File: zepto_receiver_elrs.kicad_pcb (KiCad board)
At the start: 4 copper layers, 11.2 x 7.5 mm, 44 parts, among them J1 u.fl, SW1 SW_Push, U1 STM32WLE5JBI6, U2 NCP160, U3 BGS12PL6E6327XTSA1, U4 0900FM15D0039, U5 ECS-TXO-25CSMV-320-AM-TR

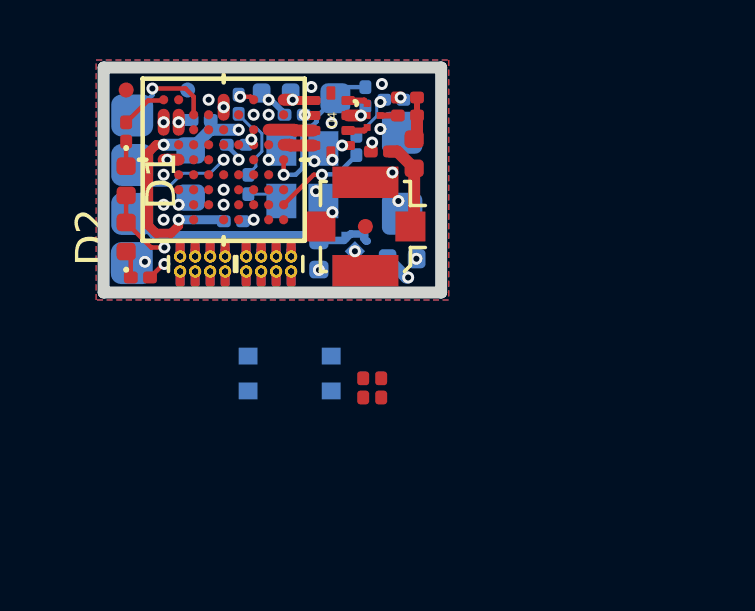
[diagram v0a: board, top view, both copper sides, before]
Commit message: updated silk screen
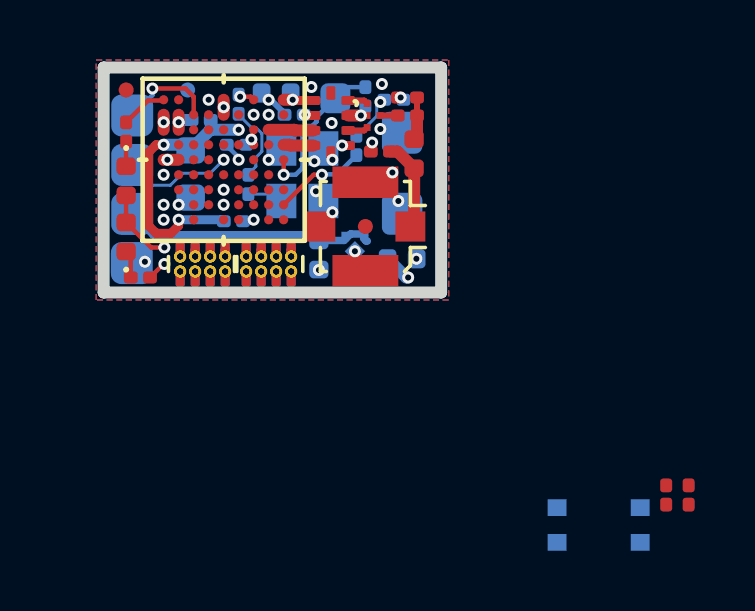
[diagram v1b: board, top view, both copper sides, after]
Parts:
- moved SW1 11.5 mm to (136.5, 66.2)
- moved R3 10.9 mm to (139.5, 65.2)
- moved C4 10.7 mm to (138.8, 65.2)
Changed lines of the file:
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@@
   (module ftprnts:0900FM15D0039 (layer F.Cu)
     (at 127.575 52.85 90)
-    (fp_text reference U4 (at 0.1 0.05 90) (layer F.SilkS)
+    (fp_text reference U4 (at 0.1 0.05 90) (layer F.SilkS) hide
       (effects (font (size 0.3 0.3) (thickness 0.05)))
     )
-    (fp_text value 0900FM15D0039 (at -0.1 -0.05 90) (layer F.Fab)
+    (fp_text value 0900FM15D0039 (at -0.1 -0.05 90) (layer F.Fab) hide
       (effects (font (size 1 1) (thickness 0.15)))
     )
@@
     (tags "SMD SMT crystal")
     (attr smd)
-    (fp_text reference U5 (at 0 2.2 90) (layer B.SilkS)
-      (effects (font (size 1 1) (thickness 0.15)) (justify mirror))
-    )
-    (fp_text value ECS-TXO-25CSMV-320-AM-TR (at 0 -2.2 90) (layer B.Fab)
+    (fp_text reference U5 (at 0 2.2 90) (layer B.SilkS) hide
+      (effects (font (size 1 1) (thickness 0.15)) (justify mirror))
+    )
+    (fp_text value ECS-TXO-25CSMV-320-AM-TR (at 0 -2.2 90) (layer B.Fab) hide
       (effects (font (size 1 1) (thickness 0.15)) (justify mirror))
     )
@@
     (fp_line (start 1.15 1) (end 1.25 0.9) (layer B.Fab) (width 0.1))
     (fp_line (start -1.15 1) (end 1.15 1) (layer B.Fab) (width 0.1))
-    (fp_text user %R (at 0 0 90) (layer B.Fab)
+    (fp_text user %R (at 0 0 90) (layer B.Fab) hide
       (effects (font (size 0.6 0.6) (thickness 0.09)) (justify mirror))
     )
@@
     (tags resistor)
     (attr smd)
-    (fp_text reference R6 (at 0 1.05 90) (layer B.SilkS)
-      (effects (font (size 1 1) (thickness 0.15)) (justify mirror))
-    )
-    (fp_text value 220R (at 0 -1.05 90) (layer B.Fab)
+    (fp_text reference R6 (at 0 1.05 90) (layer B.SilkS) hide
+      (effects (font (size 1 1) (thickness 0.15)) (justify mirror))
+    )
+    (fp_text value 220R (at 0 -1.05 90) (layer B.Fab) hide
       (effects (font (size 1 1) (thickness 0.15)) (justify mirror))
     )
@@
     (fp_line (start 0.65 0.3) (end 0.65 -0.3) (layer B.CrtYd) (width 0.05))
     (fp_line (start 0.65 -0.3) (end -0.65 -0.3) (layer B.CrtYd) (width 0.05))
-    (fp_text user %R (at 0 0.68 90) (layer B.Fab)
+    (fp_text user %R (at 0 0.68 90) (layer B.Fab) hide
       (effects (font (size 0.25 0.25) (thickness 0.04)) (justify mirror))
     )
@@
     (tags inductor)
     (attr smd)
-    (fp_text reference L1 (at 0 1.43 90) (layer B.SilkS)
-      (effects (font (size 1 1) (thickness 0.15)) (justify mirror))
-    )
-    (fp_text value 15µH (at 0 -1.43 90) (layer B.Fab)
+    (fp_text reference L1 (at 0 1.43 90) (layer B.SilkS) hide
+      (effects (font (size 1 1) (thickness 0.15)) (justify mirror))
+    )
+    (fp_text value 15µH (at 0 -1.43 90) (layer B.Fab) hide
       (effects (font (size 1 1) (thickness 0.15)) (justify mirror))
     )
@@
     (fp_line (start -0.8 0.4) (end 0.8 0.4) (layer B.Fab) (width 0.1))
     (fp_line (start -0.8 -0.4) (end -0.8 0.4) (layer B.Fab) (width 0.1))
-    (fp_text user %R (at 0 0 90) (layer B.Fab)
+    (fp_text user %R (at 0 0 90) (layer B.Fab) hide
       (effects (font (size 0.4 0.4) (thickness 0.06)) (justify mirror))
     )
@@
     (tags LED)
     (attr smd)
-    (fp_text reference D2 (at 0 -1.17 90) (layer F.SilkS)
-      (effects (font (size 1 1) (thickness 0.15)))
-    )
-    (fp_text value LED_WHITE (at 0 1.17 90) (layer F.Fab)
+    (fp_text reference D2 (at 0 -1.17 90) (layer F.SilkS) hide
+      (effects (font (size 1 1) (thickness 0.15)))
+    )
+    (fp_text value LED_WHITE (at 0 1.17 90) (layer F.Fab) hide
       (effects (font (size 1 1) (thickness 0.15)))
     )
@@
     (fp_line (start -0.5 0.25) (end -0.5 -0.25) (layer F.Fab) (width 0.1))
     (fp_circle (center -1.09 0) (end -1.04 0) (layer F.SilkS) (width 0.1))
-    (fp_text user %R (at 0 0 90) (layer F.Fab)
+    (fp_text user %R (at 0 0 90) (layer F.Fab) hide
       (effects (font (size 0.25 0.25) (thickness 0.04)))
     )
@@
     (tags LED)
     (attr smd)
-    (fp_text reference D1 (at 0 -1.17 90) (layer F.SilkS)
-      (effects (font (size 1 1) (thickness 0.15)))
-    )
-    (fp_text value LED_BLUE (at 0 1.17 90) (layer F.Fab)
+    (fp_text reference D1 (at 0 -1.17 90) (layer F.SilkS) hide
+      (effects (font (size 1 1) (thickness 0.15)))
+    )
+    (fp_text value LED_BLUE (at 0 1.17 90) (layer F.Fab) hide
       (effects (font (size 1 1) (thickness 0.15)))
     )
@@
     (fp_line (start -0.5 0.25) (end -0.5 -0.25) (layer F.Fab) (width 0.1))
     (fp_circle (center -1.09 0) (end -1.04 0) (layer F.SilkS) (width 0.1))
-    (fp_text user %R (at 0 0 90) (layer F.Fab)
+    (fp_text user %R (at 0 0 90) (layer F.Fab) hide
       (effects (font (size 0.25 0.25) (thickness 0.04)))
     )
@@
     (tags capacitor)
     (attr smd)
-    (fp_text reference C14 (at 0 1.05 90) (layer B.SilkS)
-      (effects (font (size 1 1) (thickness 0.15)) (justify mirror))
-    )
-    (fp_text value 10pF (at 0 -1.05 90) (layer B.Fab)
+    (fp_text reference C14 (at 0 1.05 90) (layer B.SilkS) hide
+      (effects (font (size 1 1) (thickness 0.15)) (justify mirror))
+    )
+    (fp_text value 10pF (at 0 -1.05 90) (layer B.Fab) hide
       (effects (font (size 1 1) (thickness 0.15)) (justify mirror))
     )
@@
     (fp_line (start -0.3 0.15) (end 0.3 0.15) (layer B.Fab) (width 0.1))
     (fp_line (start -0.3 -0.15) (end -0.3 0.15) (layer B.Fab) (width 0.1))
-    (fp_text user %R (at 0 0.68 90) (layer B.Fab)
+    (fp_text user %R (at 0 0.68 90) (layer B.Fab) hide
       (effects (font (size 0.25 0.25) (thickness 0.04)) (justify mirror))
     )
@@
   )
   (module ftprnts:EVPBL9A2B000 (layer B.Cu)
-    (at 126.2 61.2 180)
+    (at 136.5 66.25 180)
     (fp_text reference SW1 (at 0.55069 2.13777 180) (layer B.SilkS) hide
       (effects (font (size 1.001291 1.001291) (thickness 0.015)) (justify mirror))
@@
   )
   (module ftprnts:R_0201_0603Metric_dense (layer F.Cu)
-    (at 129.25 61.68 90)
+    (at 139.5 65.25 90)
     (descr "Resistor SMD 0201 (0603 Metric), square (rectangular) end terminal, IPC_7351 nominal, (Body size source: https://www.vishay.com/docs/20052/crcw0201e3.pdf), generated with kicad-footprint-generator")
     (tags resistor)
@@
   )
   (module ftprnts:C_0201_0603Metric_dense (layer F.Cu)
-    (at 128.65 61.68 90)
+    (at 138.75 65.25 90)
     (descr "Capacitor SMD 0201 (0603 Metric), square (rectangular) end terminal, IPC_7351 nominal, (Body size source: https://www.vishay.com/docs/20052/crcw0201e3.pdf), generated with kicad-footprint-generator")
     (tags capacitor)
